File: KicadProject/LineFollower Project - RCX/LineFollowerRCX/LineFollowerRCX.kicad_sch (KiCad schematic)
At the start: 15 parts, among them J1 Conn_01x11_Pin, J10 GND pinos, J2 Motor 1, J3 Motor 1, J4 Modulo bluetooth, J5 Sensor Lateral - Esquerda, J6 Sensor Lateral - Direita, J7 Conector sensor lateral Esque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, J8 Conector sensor lateral Direi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, J9 VCC pinos, U1 ROB-14450, U2 LM7805_TO220

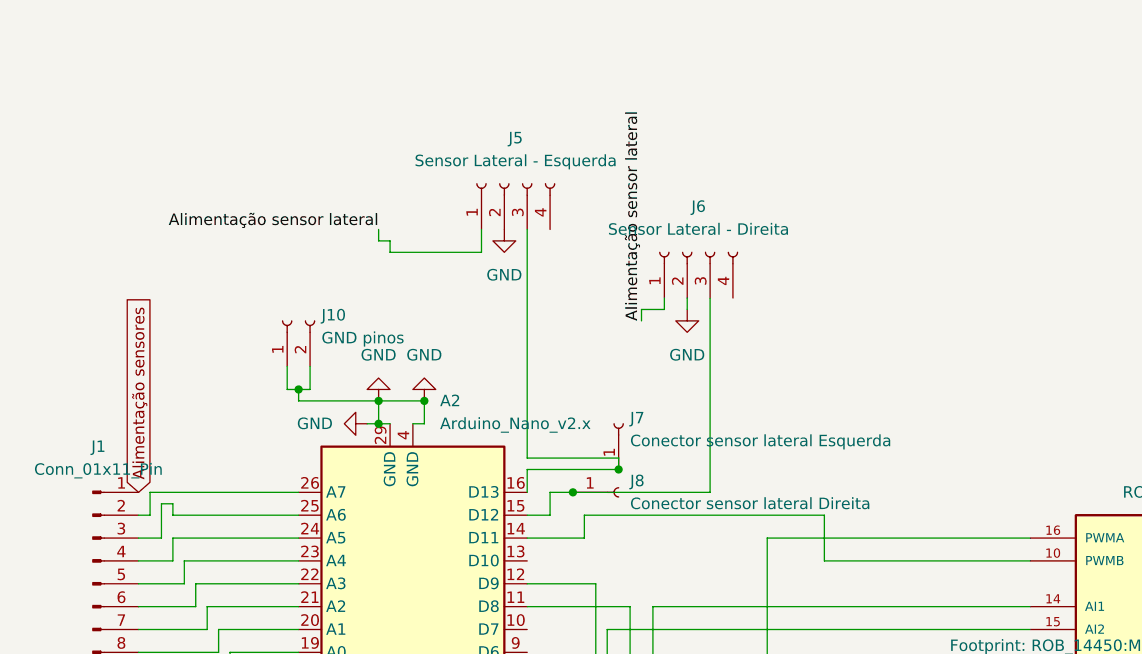
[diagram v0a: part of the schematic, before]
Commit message: fix: remove sensor lateral esquerdo do esquemático
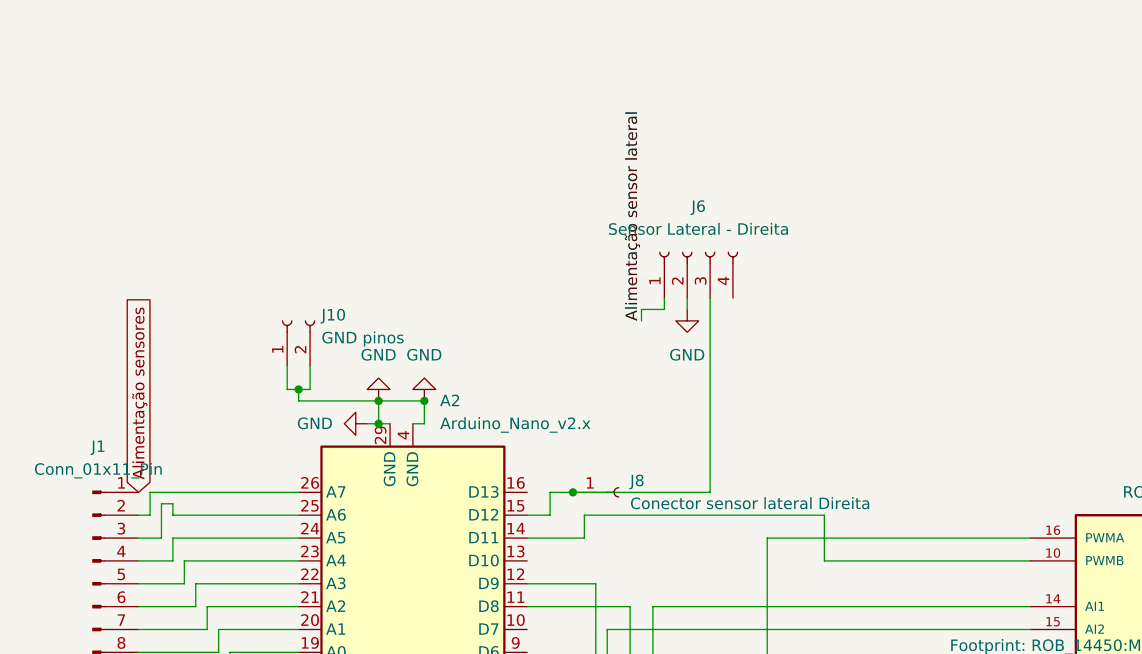
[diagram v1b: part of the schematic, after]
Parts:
- removed J5: Sensor Lateral - Esquerda, Connector_PinSocket_2.54mm:PinSocket_1x04_P2.54mm_Horizontal, symbol Connector:Conn_01x04_Socket
- removed J7: Conector sensor lateral Esquerda, Connector_PinSocket_2.54mm:PinSocket_1x01_P2.54mm_Vertical, symbol Connector:Conn_01x01_Socket

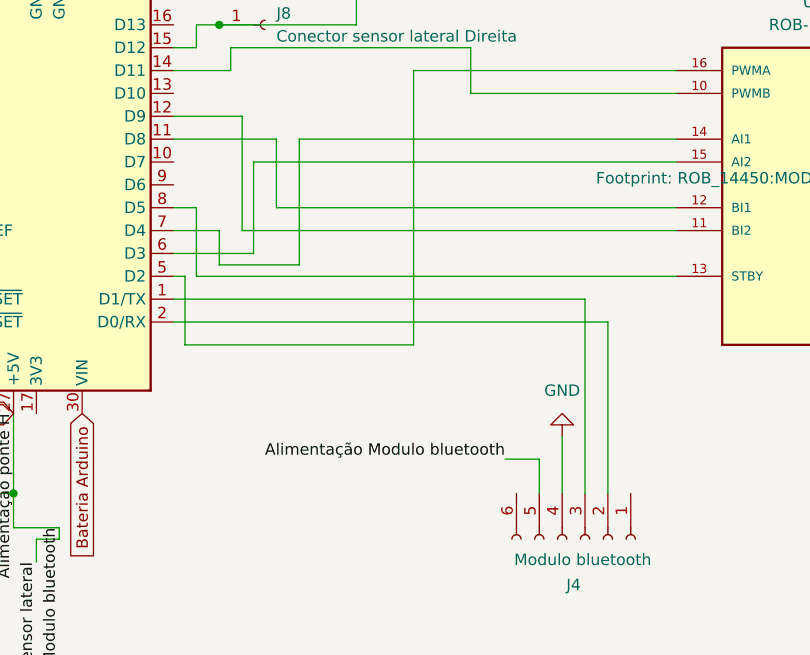
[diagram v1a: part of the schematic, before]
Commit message: altera dimensões da placa & ajusta posições dos componentes
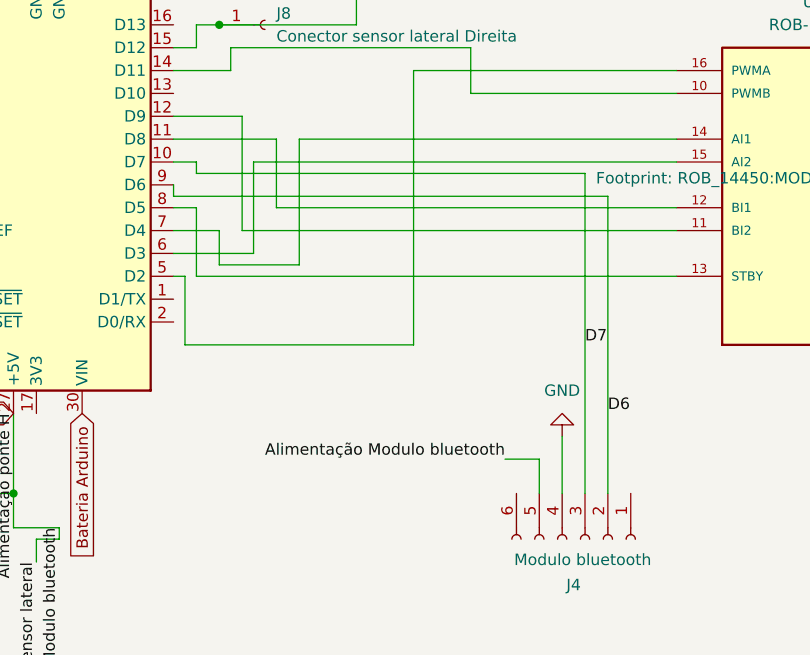
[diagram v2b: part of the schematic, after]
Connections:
- net at A2.2 (D0/RX): no longer J4.2 (RX)
- net at A2.1 (D1/TX): no longer J4.3 (TX)
- net D7: now reaches A2.10 (D7)
- net D7: now also J4.3 (TX)
- net D6: now reaches A2.9 (D6)
- net D6: now also J4.2 (RX)
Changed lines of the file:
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@@
+	(wire
+		(pts
+			(xy 123.19 140.97) (xy 123.19 105.41)
+		)
+		(stroke
+			(width 0)
+			(type default)
+		)
+	)
 	(wire
 		(pts
@@
 	(wire
 		(pts
-			(xy 77.47 119.38) (xy 123.19 119.38)
-		)
-		(stroke
-			(width 0)
-			(type default)
-		)
-	)
-	(wire
-		(pts
 			(xy 52.07 77.47) (xy 50.8 77.47)
 		)
@@
 	(wire
 		(pts
+			(xy 77.47 107.95) (xy 77.47 106.68)
+		)
+		(stroke
+			(width 0)
+			(type default)
+		)
+	)
+	(wire
+		(pts
 			(xy 133.35 93.98) (xy 104.14 93.98)
 		)
@@
 	(wire
 		(pts
+			(xy 125.73 107.95) (xy 77.47 107.95)
+		)
+		(stroke
+			(width 0)
+			(type default)
+		)
+	)
+	(wire
+		(pts
 			(xy 60.96 81.28) (xy 62.23 81.28)
 		)
@@
 	(wire
 		(pts
+			(xy 123.19 105.41) (xy 80.01 105.41)
+		)
+		(stroke
+			(width 0)
+			(type default)
+		)
+	)
+	(wire
+		(pts
 			(xy 39.37 96.52) (xy 39.37 99.06)
 		)
@@
 	(wire
 		(pts
+			(xy 80.01 105.41) (xy 80.01 104.14)
+		)
+		(stroke
+			(width 0)
+			(type default)
+		)
+	)
+	(wire
+		(pts
 			(xy 59.69 140.97) (xy 59.69 144.78)
 		)
@@
 	(wire
 		(pts
-			(xy 123.19 119.38) (xy 123.19 140.97)
-		)
-		(stroke
-			(width 0)
-			(type default)
-		)
-	)
-	(wire
-		(pts
 			(xy 41.91 101.6) (xy 41.91 104.14)
 		)
@@
 	(wire
 		(pts
-			(xy 77.47 121.92) (xy 125.73 121.92)
-		)
-		(stroke
-			(width 0)
-			(type default)
-		)
-	)
-	(wire
-		(pts
 			(xy 66.04 78.74) (xy 66.04 81.28)
 		)
@@
 	(wire
 		(pts
-			(xy 125.73 121.92) (xy 125.73 140.97)
-		)
-		(stroke
-			(width 0)
-			(type default)
-		)
-	)
-	(wire
-		(pts
 			(xy 186.69 77.47) (xy 186.69 78.74)
 		)
@@
 	(wire
 		(pts
+			(xy 125.73 140.97) (xy 125.73 107.95)
+		)
+		(stroke
+			(width 0)
+			(type default)
+		)
+	)
+	(wire
+		(pts
 			(xy 85.09 99.06) (xy 77.47 99.06)
 		)
@@
 	(wire
 		(pts
+			(xy 80.01 104.14) (xy 77.47 104.14)
+		)
+		(stroke
+			(width 0)
+			(type default)
+		)
+	)
+	(wire
+		(pts
 			(xy 85.09 111.76) (xy 85.09 99.06)
 		)
@@
 		)
 	)
+	(label "D7"
+		(at 123.19 124.46 0)
+		(fields_autoplaced yes)
+		(effects
+			(font
+				(size 1.27 1.27)
+			)
+			(justify left bottom)
+		)
+	)
+	(label "D6"
+		(at 125.73 132.08 0)
+		(fields_autoplaced yes)
+		(effects
+			(font
+				(size 1.27 1.27)
+			)
+			(justify left bottom)
+		)
+	)

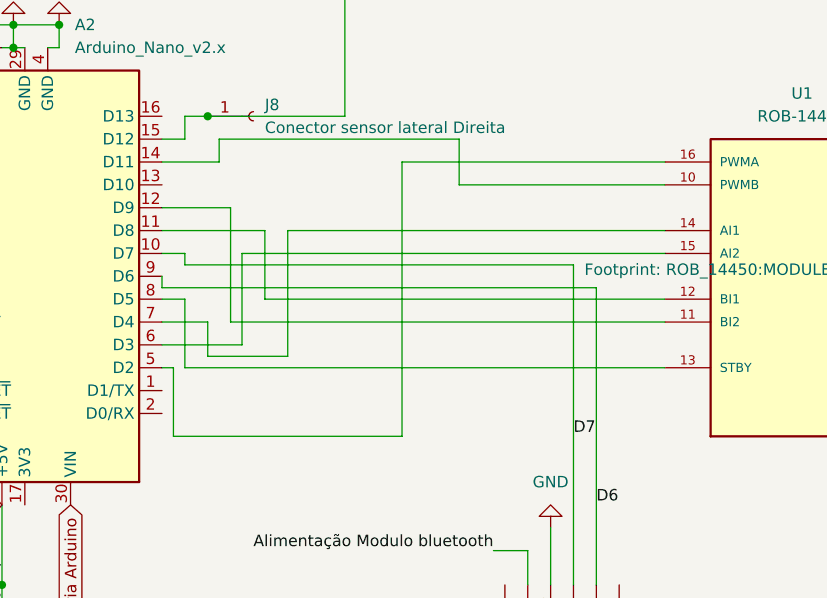
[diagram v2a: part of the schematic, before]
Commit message: fix: troca porta PWMA da ponte h para pino 10
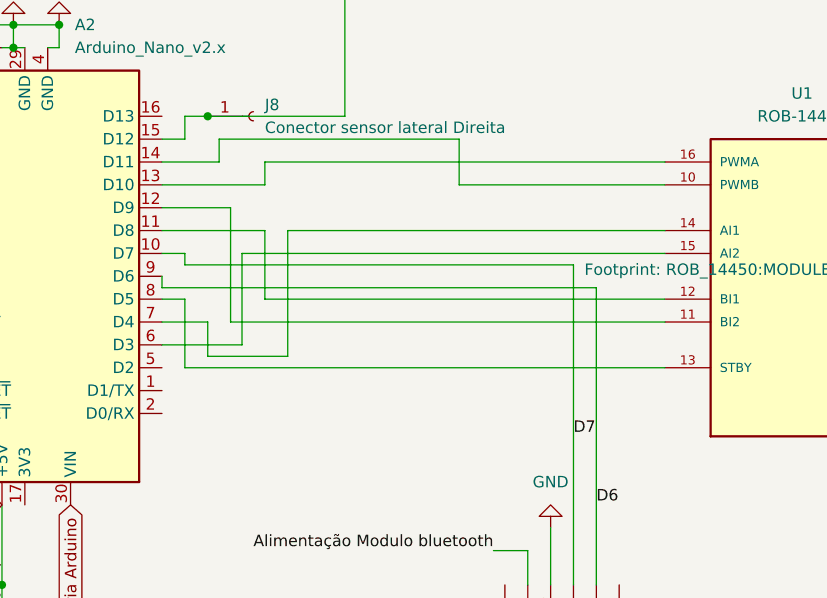
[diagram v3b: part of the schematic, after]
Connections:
- net at U1.16 (PWMA): now also A2.13 (D10); no longer A2.5 (D2)
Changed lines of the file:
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@@
-	(wire
-		(pts
-			(xy 78.74 124.46) (xy 78.74 116.84)
-		)
-		(stroke
-			(width 0)
-			(type default)
-		)
-	)
 	(wire
 		(pts
@@
 	(wire
 		(pts
+			(xy 88.9 93.98) (xy 88.9 96.52)
+		)
+		(stroke
+			(width 0)
+			(type default)
+		)
+	)
+	(wire
+		(pts
 			(xy 38.1 90.17) (xy 36.83 90.17)
 		)
@@
 	(wire
 		(pts
+			(xy 88.9 96.52) (xy 77.47 96.52)
+		)
+		(stroke
+			(width 0)
+			(type default)
+		)
+	)
+	(wire
+		(pts
 			(xy 36.83 90.17) (xy 36.83 93.98)
 		)
@@
 	(wire
 		(pts
-			(xy 104.14 124.46) (xy 78.74 124.46)
-		)
-		(stroke
-			(width 0)
-			(type default)
-		)
-	)
-	(wire
-		(pts
 			(xy 123.19 140.97) (xy 123.19 105.41)
 		)
@@
 	(wire
 		(pts
-			(xy 133.35 93.98) (xy 104.14 93.98)
-		)
-		(stroke
-			(width 0)
-			(type default)
-		)
-	)
-	(wire
-		(pts
 			(xy 185.42 111.76) (xy 185.42 116.84)
 		)
@@
 	(wire
 		(pts
-			(xy 78.74 116.84) (xy 77.47 116.84)
-		)
-		(stroke
-			(width 0)
-			(type default)
-		)
-	)
-	(wire
-		(pts
 			(xy 165.1 93.98) (xy 163.83 93.98)
 		)
@@
 	(wire
 		(pts
+			(xy 88.9 93.98) (xy 133.35 93.98)
+		)
+		(stroke
+			(width 0)
+			(type default)
+		)
+	)
+	(wire
+		(pts
 			(xy 52.07 96.52) (xy 39.37 96.52)
 		)
@@
 		)
 		(stroke
-			(width 0)
-			(type default)
-		)
-	)
-	(wire
-		(pts
-			(xy 104.14 93.98) (xy 104.14 124.46)
-		)
-		(stroke

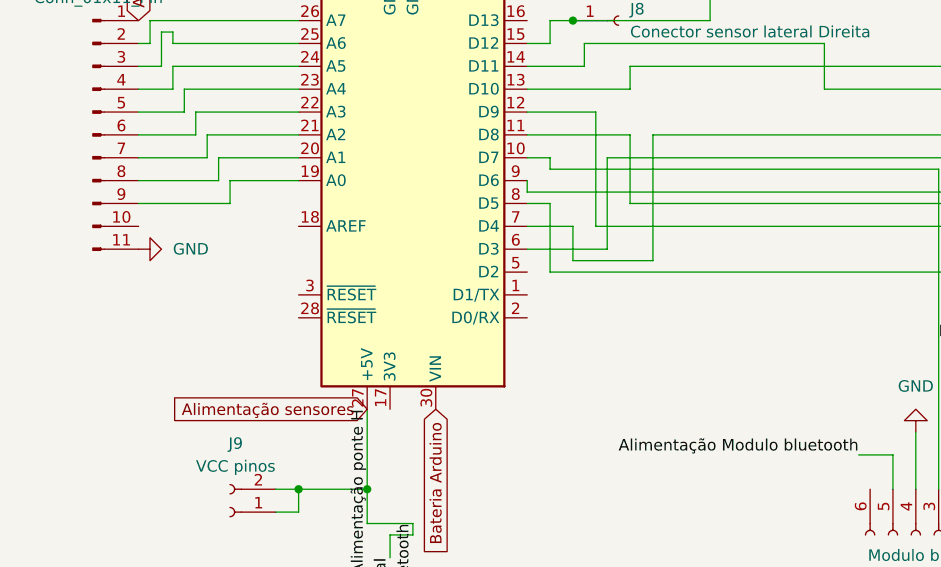
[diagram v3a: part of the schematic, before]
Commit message: fix: arrumando espaçãmento da bateria robô
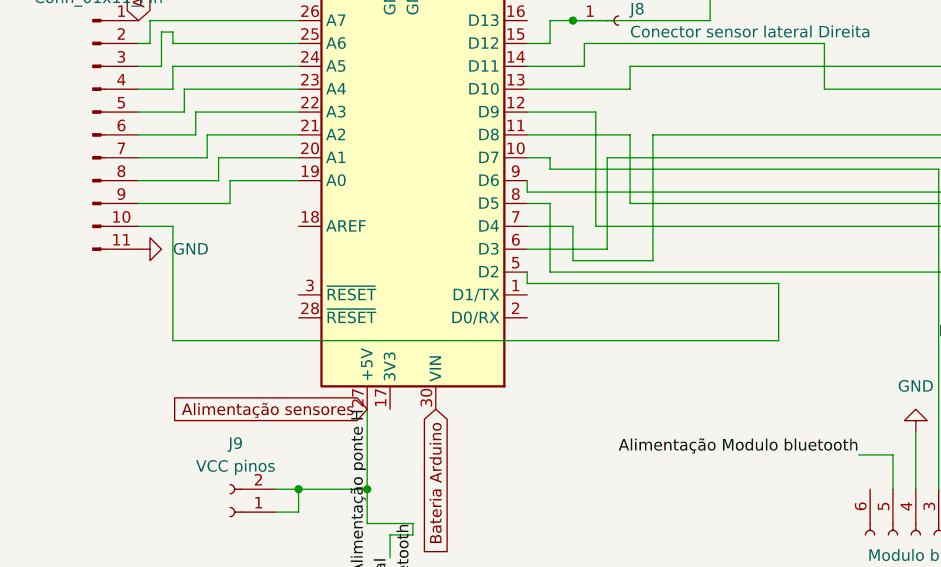
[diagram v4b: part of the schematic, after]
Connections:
- net at J1.10 (Pin_10): now also A2.5 (D2)
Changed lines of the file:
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@@
+	(wire
+		(pts
+			(xy 105.41 124.46) (xy 38.1 124.46)
+		)
+		(stroke
+			(width 0)
+			(type default)
+		)
+	)
 	(wire
 		(pts
@@
 	(wire
 		(pts
+			(xy 38.1 111.76) (xy 34.29 111.76)
+		)
+		(stroke
+			(width 0)
+			(type default)
+		)
+	)
+	(wire
+		(pts
 			(xy 38.1 96.52) (xy 34.29 96.52)
 		)
@@
 	(wire
 		(pts
+			(xy 38.1 124.46) (xy 38.1 111.76)
+		)
+		(stroke
+			(width 0)
+			(type default)
+		)
+	)
+	(wire
+		(pts
 			(xy 88.9 101.6) (xy 77.47 101.6)
 		)
@@
 	(wire
 		(pts
+			(xy 77.47 116.84) (xy 77.47 118.11)
+		)
+		(stroke
+			(width 0)
+			(type default)
+		)
+	)
+	(wire
+		(pts
+			(xy 77.47 118.11) (xy 105.41 118.11)
+		)
+		(stroke
+			(width 0)
+			(type default)
+		)
+	)
+	(wire
+		(pts
 			(xy 66.04 78.74) (xy 66.04 81.28)
 		)
@@
 		)
 		(stroke
+			(width 0)
+			(type default)
+		)
+	)
+	(wire
+		(pts
+			(xy 105.41 118.11) (xy 105.41 124.46)
+		)
+		(stroke
